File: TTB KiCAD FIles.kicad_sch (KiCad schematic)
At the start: 5 parts, among them J1 PJ-102A, U1 Relay Control Module, U2 ESP32 Module, U3 Motor Driver Module, U4 Pololu_Voltage_Regulator

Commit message: Updates
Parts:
- added J2: Conn_01x03_Pin, Connector_PinHeader_2.54mm:PinHeader_1x03_P2.54mm_Vertical, symbol Connector:Conn_01x03_Pin
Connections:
- net +12V: now also J2.2 (Pin_2)
- net +5V: now also J2.3 (Pin_3)
- net GND: now also J2.1 (Pin_1)

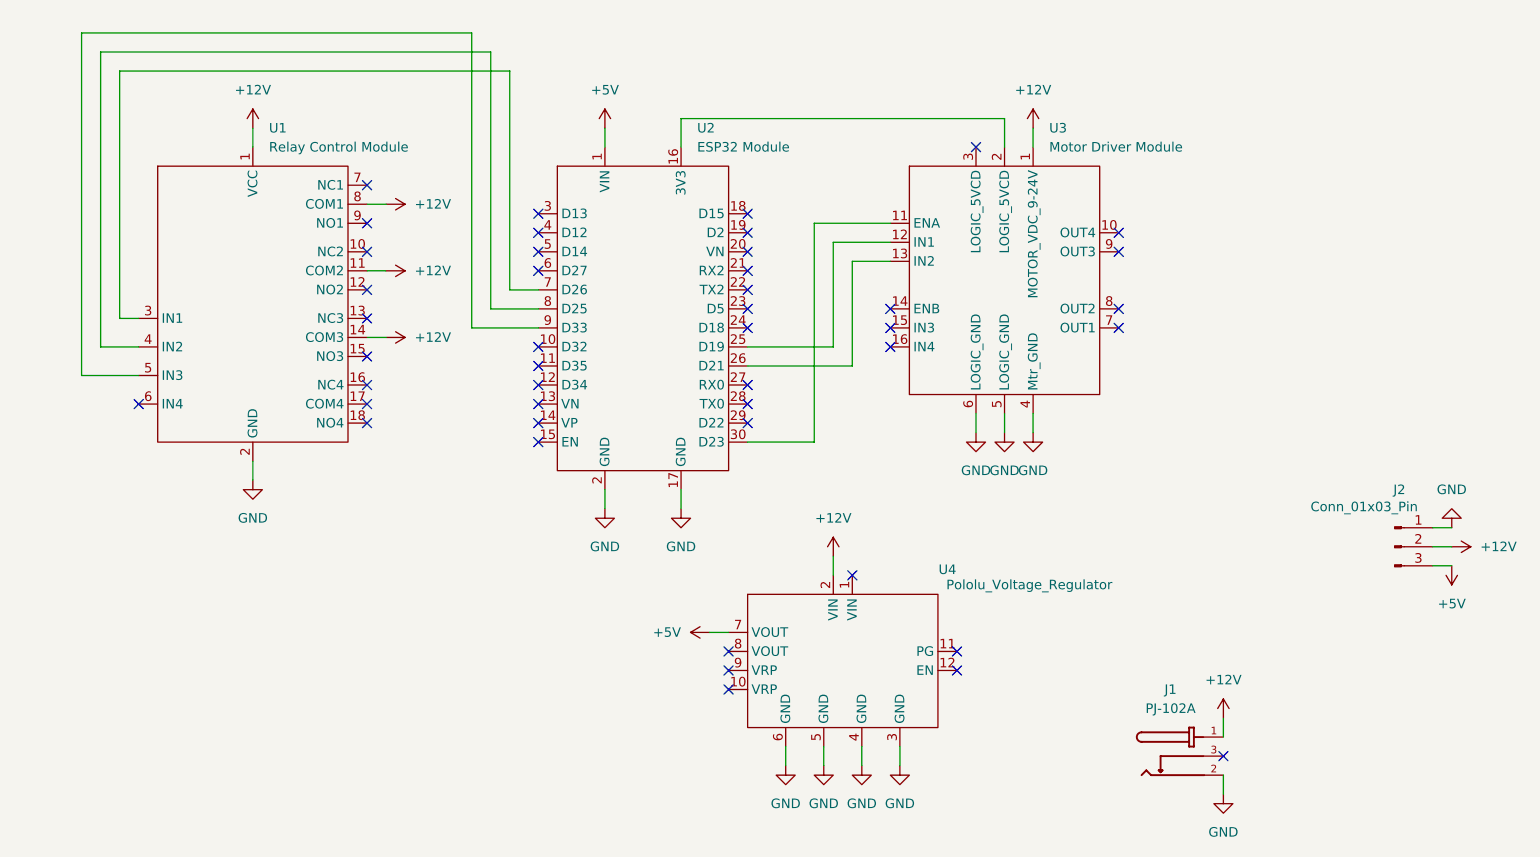
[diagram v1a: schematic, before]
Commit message: Added Design Modifications
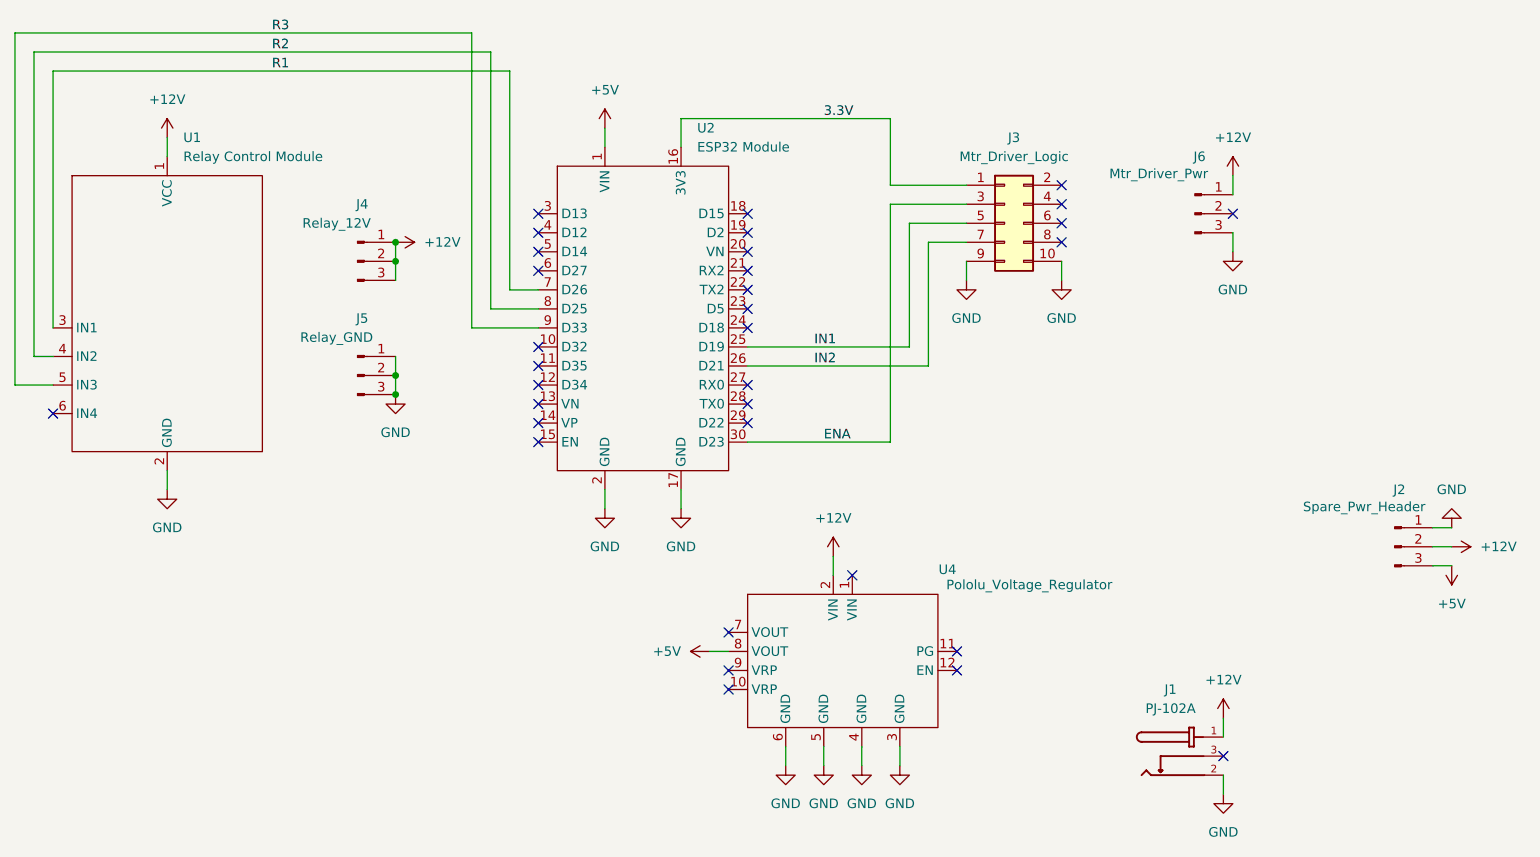
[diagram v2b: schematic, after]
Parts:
- removed U3: Motor Driver Module, TTB KiCAD Footprints:XY-160D Motor Driver, symbol TTB KiCAD Components:XY-160D_Motor_Driver
- added J3: Mtr_Driver_Logic, Connector_PinHeader_2.54mm:PinHeader_2x05_P2.54mm_Vertical, symbol Connector_Generic:Conn_02x05_Odd_Even
- added J4: Relay_12V, Connector_PinHeader_2.54mm:PinHeader_1x03_P2.54mm_Vertical, symbol Connector:Conn_01x03_Pin
- added J5: Relay_GND, Connector_PinHeader_2.54mm:PinHeader_1x03_P2.54mm_Vertical, symbol Connector:Conn_01x03_Pin
- added J6: Mtr_Driver_Pwr, Connector_PinHeader_2.54mm:PinHeader_1x03_P2.54mm_Vertical, symbol Connector:Conn_01x03_Pin
- J2: value Conn_01x03_Pin -> Spare_Pwr_Header
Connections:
- net +12V: now also J4.1 (Pin_1), J4.2 (Pin_2), J4.3 (Pin_3), J6.1 (Pin_1); no longer U1.11 (COM2), U1.14 (COM3), U1.8 (COM1)
- net +5V: now also U4.8 (VOUT); no longer U4.7 (VOUT)
- net GND: now also J3.10 (Pin_10), J3.9 (Pin_9), J5.1 (Pin_1), J5.2 (Pin_2), J5.3 (Pin_3), J6.3 (Pin_3)
- net R1: now reaches U1.3 (IN1), U2.7 (D26)
- net R2: now reaches U1.4 (IN2), U2.8 (D25)
- net R3: now reaches U1.5 (IN3), U2.9 (D33)
- net ENA: now reaches U2.30 (D23)
- net ENA: now also J3.3 (Pin_3)
- net IN1: now reaches U2.25 (D19)
- net IN1: now also J3.5 (Pin_5)
- net IN2: now reaches U2.26 (D21)
- net IN2: now also J3.7 (Pin_7)
- net 3.3V : now reaches U2.16 (3V3)
- net 3.3V : now also J3.1 (Pin_1)
- no-connect marks 45 -> 33

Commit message: Clean up draw.io files & kicad files
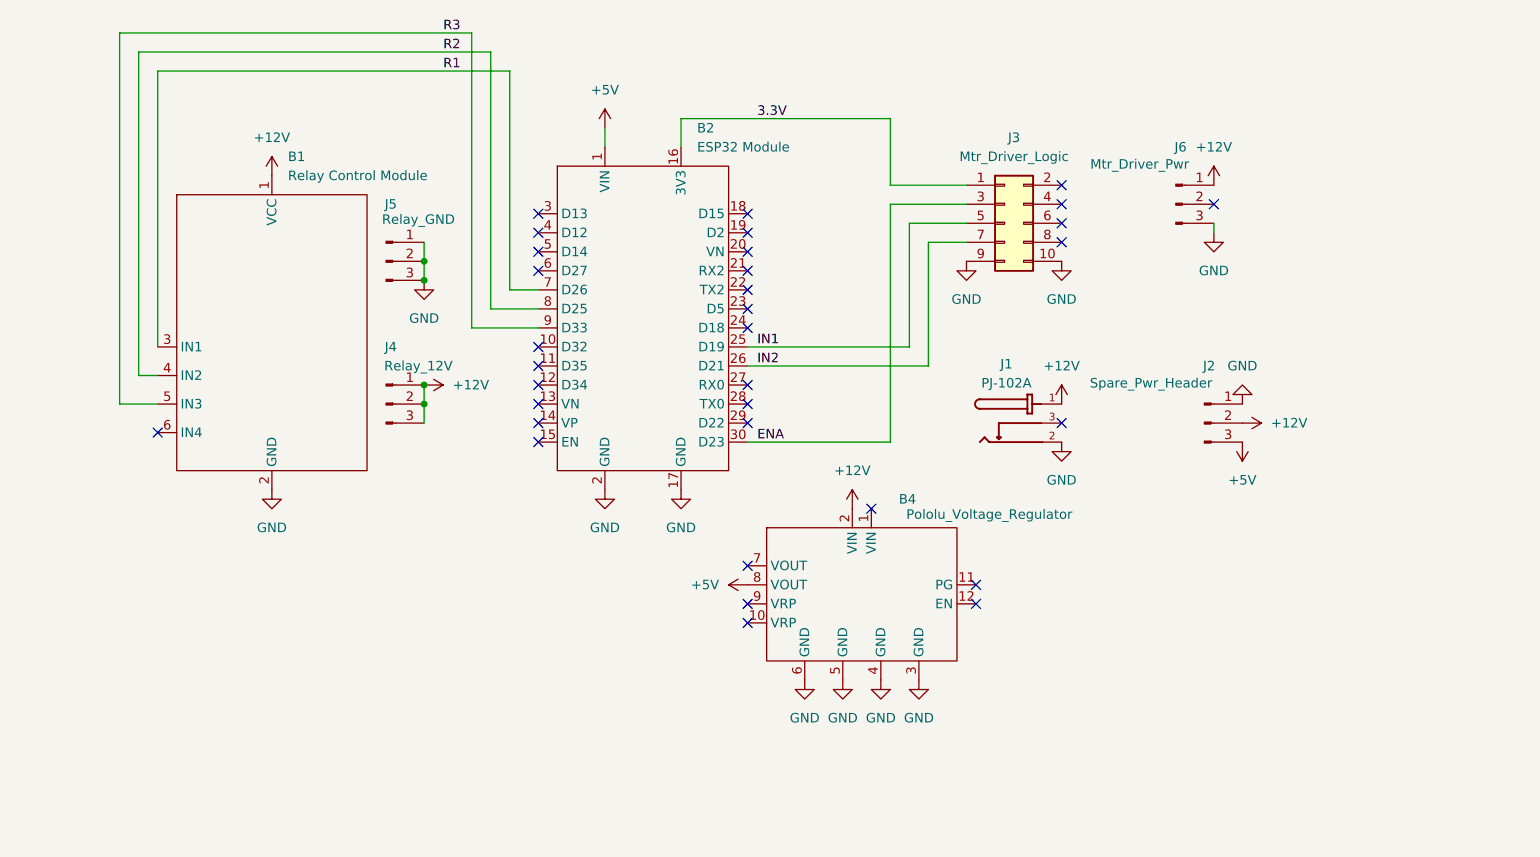
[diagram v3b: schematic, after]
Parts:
- renumbered U1 to B1, U2 to B2, U4 to B4
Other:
- moved on the sheet: B1, B4, J1, J2, J4, J5, J6
